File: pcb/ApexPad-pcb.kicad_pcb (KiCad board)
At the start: 2 copper layers, 90.2 x 55 mm, 15 parts, among them J1 OLED_DISPLAY, SW2 SW_Push_45deg, SW3 SW_Push_45deg, SW4 SW_Push_45deg, SW5 SW_Push_45deg, U1 Seeed Studio XIAO RP2040

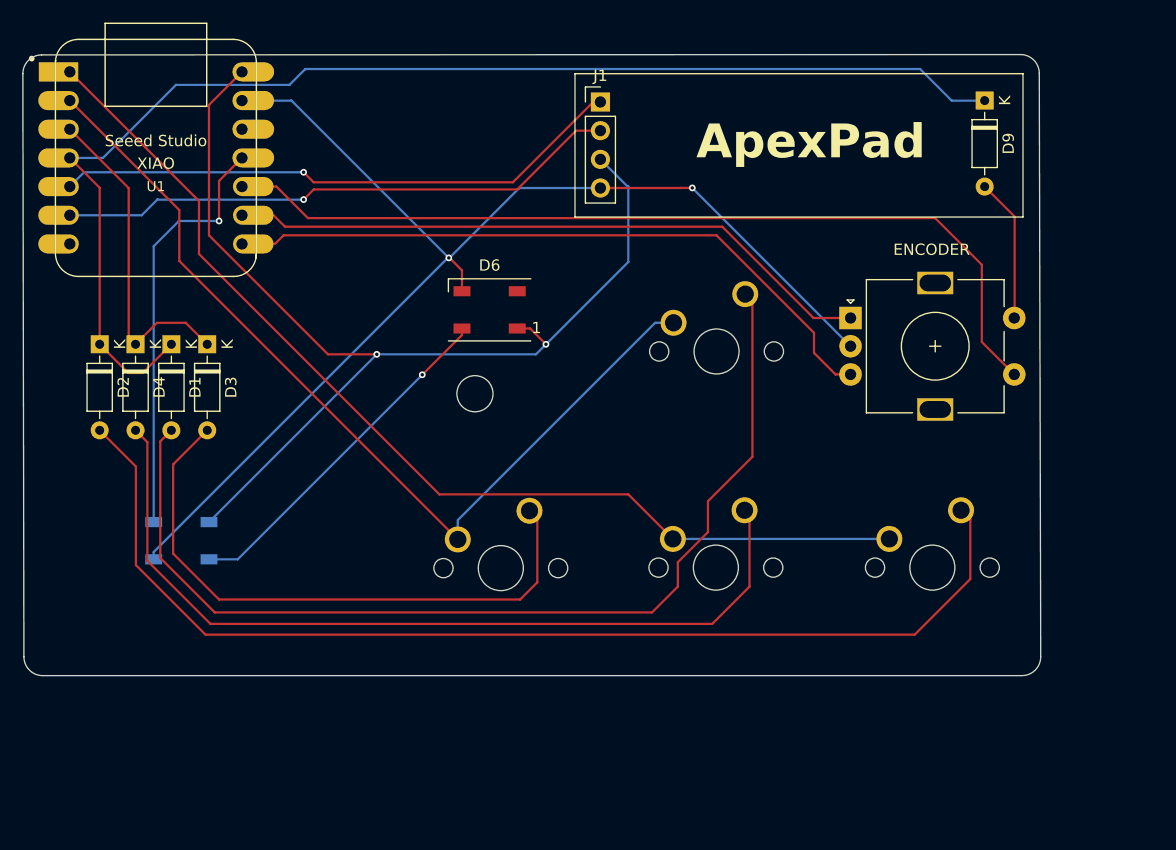
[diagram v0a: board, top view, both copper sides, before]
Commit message: Redid PCB and Made it Smaller
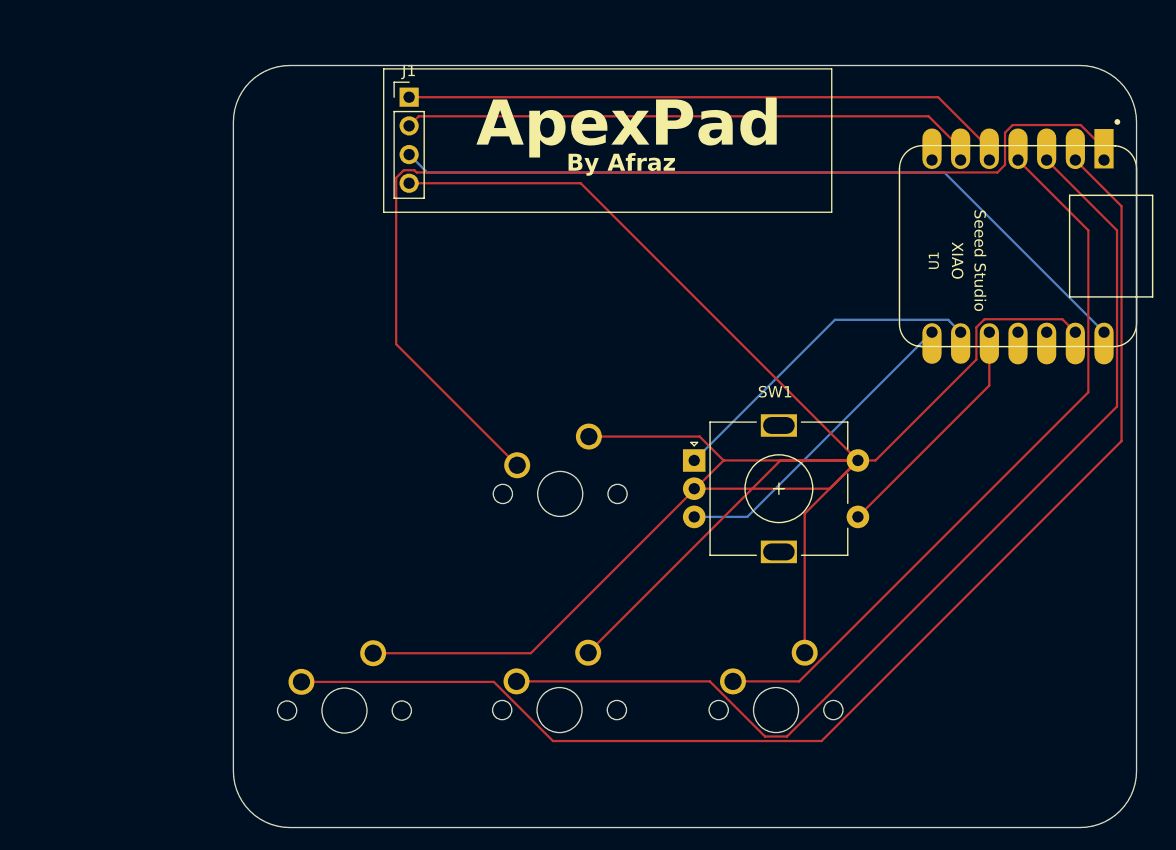
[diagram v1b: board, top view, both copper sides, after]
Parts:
- removed D1, D2, D3, D4, D9: D, Diode_THT:D_DO-35_SOD27_P7.62mm_Horizontal
- removed D5, D6: WS2812B, LED_SMD:LED_WS2812B_PLCC4_5.0x5.0mm_P3.2mm
- removed REF**: MountingHole_3.2mm_M3, MountingHole:MountingHole_3.2mm_M3
- moved U1 76.8 mm to (188.5, 91.0), turned to -90 degrees
- moved SW1 18.7 mm to (159.8, 110.0)
- moved SW3 18.7 mm to (128.8, 132.1)
- moved SW2 18.7 mm to (147.9, 112.9)
- moved SW4 18.7 mm to (147.9, 132.1)
- moved SW5 18.7 mm to (167.1, 132.1)
- moved J1 16.9 mm to (134.6, 77.8)
- renumbered ENCODER to SW1
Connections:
- net COL2 renamed EC11SWB
- SW1 pad S2: EC11SWA -> GND
- SW2 pad 1: COL0 -> SW2
- SW2 pad 2: Net-(D1-A) -> GND
- SW3 pad 1: COL0 -> SW3
- SW3 pad 2: Net-(D3-A) -> GND
- SW4 pad 1: COL1 -> SW4
- SW4 pad 2: Net-(D4-A) -> GND
- SW5 pad 1: COL1 -> SW5
- SW5 pad 2: Net-(D2-A) -> GND
- U1 pad 1: COL1 -> SW2
- U1 pad 2: COL0 -> SW3
- U1 pad 3: ROW1 -> SW4
- U1 pad 4: ROW0 -> SW5
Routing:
- net SW3: track 0.00 -> 112.4 mm
- net ROW0: track 111.5 -> 0.00 mm
- net SW2: track 0.00 -> 98.3 mm
- net Net-(D2-A): track 98.2 -> 0.00 mm
- net GND: track 109.1 -> 204.8 mm, vias 2 -> 0
- net COL1: track 92.5 -> 0.00 mm
- net SW4: track 0.00 -> 91.7 mm
- net Net-(D1-A): track 89.4 -> 0.00 mm
- net COL0: track 81.2 -> 0.00 mm
- net Net-(D4-A): track 76.0 -> 0.00 mm
- net SW5: track 0.00 -> 65.2 mm
- net EC11SWB: track 79.3 -> 21.2 mm
- net Net-(D3-A): track 53.4 -> 0.00 mm
- net WS2812B: track 37.6 -> 0.00 mm, vias 1 -> 0
- net EC11B: track 60.4 -> 27.8 mm
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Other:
- board size 90.2 x 55 mm -> 80 x 67.5 mm
- board text added: "By Afraz"
- board text removed: "12mm"
- board text removed: "14mm"
